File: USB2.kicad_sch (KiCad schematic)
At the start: 5 parts, among them J301 USB_C_Receptacle_USB2.0, U301 RCLAMP0524P

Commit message: Fix schematic ERC errors
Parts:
- U301: footprint Package_SON:USON-10_2.5x1.0mm_P0.5mm -> Package_DFN_QFN:Diodes_UDFN-10_1.0x2.5mm_P0.5mm; symbol Yellow:TPD4EUSB30 -> Hatlabs:RCLAMP0524P
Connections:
- net USB.D+: no longer U301.9 (D1-)
- net USB.D-: no longer U301.10 (D1+)
- net VBUS: no longer U301.7 (D2+)
- net at U301.5: no longer U301.6 (D2-)
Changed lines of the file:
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@@
-			)
-		)
-		(property "Sim.Enable" ""
-			(at 138.43 68.58 0)
-			(effects
-				(font
-					(size 1.27 1.27)
-				)
 			)
 		)
@@
 	)
 	(symbol
-		(lib_name "Yellow:TPD4EUSB30_1")
-		(lib_id "Yellow:TPD4EUSB30")
+		(lib_id "Hatlabs:RCLAMP0524P")
 		(at 163.83 121.92 0)
 		(unit 1)
@@
 			)
 		)
-		(property "Footprint" "Package_SON:USON-10_2.5x1.0mm_P0.5mm"
+		(property "Footprint" "Package_DFN_QFN:Diodes_UDFN-10_1.0x2.5mm_P0.5mm"
 			(at 139.7 132.08 0)
 			(effects
@@
 			)
 		)
-		(property "Description" ""
+		(property "Description" "4-Channel Low Capacitance TVS Diode Array, DFN-10"
 			(at 163.83 121.92 0)
 			(effects
@@
 					(size 1.27 1.27)
 				)
-			)
-		)
-		(property "Sim.Enable" ""
-			(at 163.83 121.92 0)
-			(effects
-				(font
-					(size 1.27 1.27)
-				)
+				(hide yes)
 			)
 		)
@@
 			)
 		)
-		(property "Sim.Enable" ""
-			(at 119.38 66.04 0)
-			(effects
-				(font
-					(size 1.27 1.27)
-				)
-			)
-		)
 		(pin "1"
 		)
@@
 			)
 		)
-		(property "Sim.Enable" ""
-			(at 138.43 66.04 0)
-			(effects
-				(font
-					(size 1.27 1.27)
-				)
-			)
-		)
 		(pin "1"
 		)
@@
 			(at 165.1 76.2 0)
 			(effects
-				(font
-					(size 1.27 1.27)
-				)
-			)
-		)
-		(property "Sim.Enable" ""
-			(at 165.1 76.2 0)
-			(effects

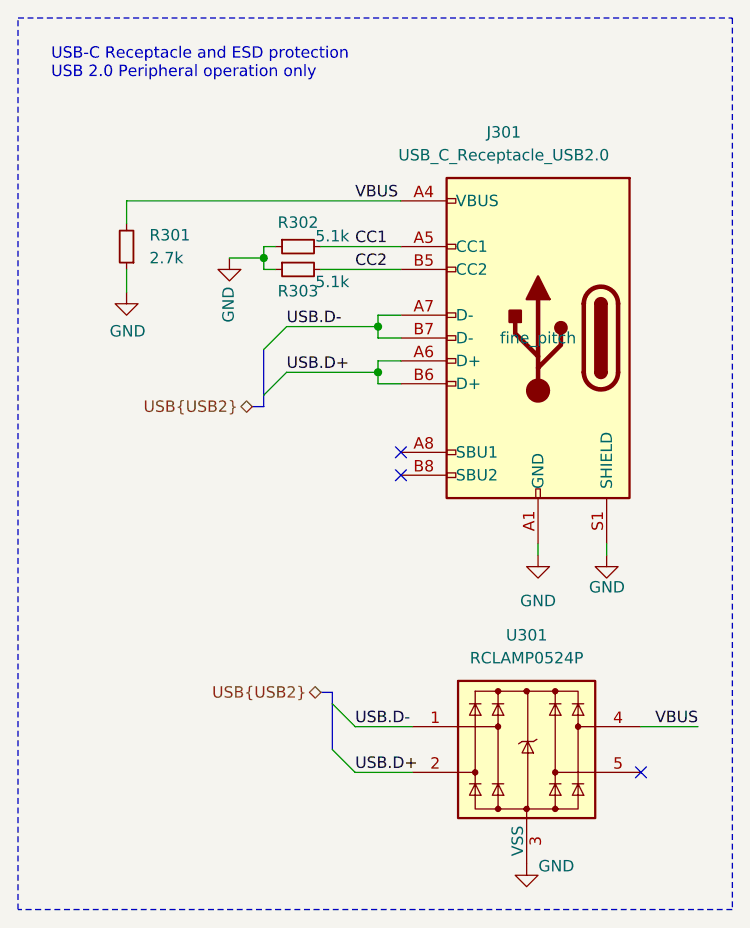
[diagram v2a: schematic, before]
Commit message: Reannotate components
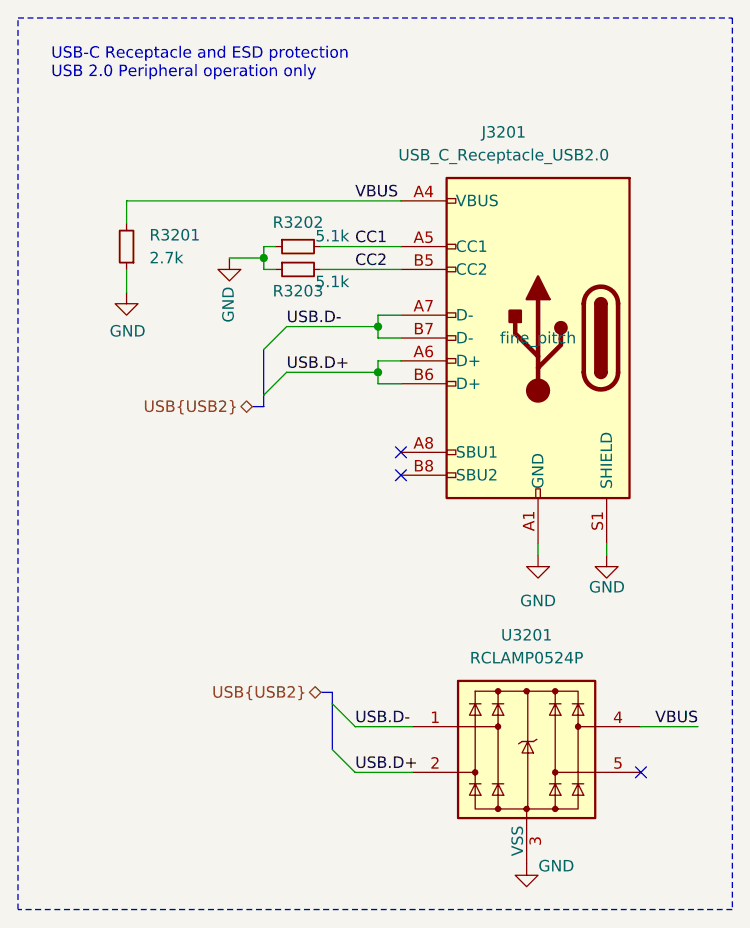
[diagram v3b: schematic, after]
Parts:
- renumbered J301 to J3201, R301 to R3201, R302 to R3202, R303 to R3203, U301 to U3201
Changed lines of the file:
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@@
 		(on_board yes)
 		(dnp no)
-		(property "Reference" "#PWR0301"
+		(property "Reference" "#PWR03202"
 			(at 130.81 73.66 0)
 			(effects
@@
 			(project "HALPI2"
 				(path "/abc482bd-3f17-4d35-80db-1da3dcdb5c27/aa1d8d83-5167-420c-9ee7-3e4dcc942bfc"
-					(reference "#PWR0301")
+					(reference "#PWR03202")
 					(unit 1)
 				)
@@
 		(on_board yes)
 		(dnp no)
-		(property "Reference" "R303"
+		(property "Reference" "R3203"
 			(at 138.43 70.9868 90)
 			(effects
@@
 			(project "HALPI2"
 				(path "/abc482bd-3f17-4d35-80db-1da3dcdb5c27/aa1d8d83-5167-420c-9ee7-3e4dcc942bfc"
-					(reference "R303")
+					(reference "R3203")
 					(unit 1)
 				)
@@
 		(dnp no)
 		(fields_autoplaced yes)
-		(property "Reference" "#PWR0303"
+		(property "Reference" "#PWR03204"
 			(at 165.1 106.68 0)
 			(effects
@@
 			(project "HALPI2"
 				(path "/abc482bd-3f17-4d35-80db-1da3dcdb5c27/aa1d8d83-5167-420c-9ee7-3e4dcc942bfc"
-					(reference "#PWR0303")
+					(reference "#PWR03204")
 					(unit 1)
 				)
@@
 		(on_board yes)
 		(dnp no)
-		(property "Reference" "#PWR0304"
+		(property "Reference" "#PWR03205"
 			(at 172.72 106.68 0)
 			(effects
@@
 			(project "HALPI2"
 				(path "/abc482bd-3f17-4d35-80db-1da3dcdb5c27/aa1d8d83-5167-420c-9ee7-3e4dcc942bfc"
-					(reference "#PWR0304")
+					(reference "#PWR03205")
 					(unit 1)
 				)
@@
 		(on_board yes)
 		(dnp no)
-		(property "Reference" "U301"
+		(property "Reference" "U3201"
 			(at 163.83 109.22 0)
 			(effects
@@
 			(project "HALPI2"
 				(path "/abc482bd-3f17-4d35-80db-1da3dcdb5c27/aa1d8d83-5167-420c-9ee7-3e4dcc942bfc"
-					(reference "U301")
+					(reference "U3201")
 					(unit 1)
 				)
@@
 		(dnp no)
 		(fields_autoplaced yes)
-		(property "Reference" "R301"
+		(property "Reference" "R3201"
 			(at 121.92 64.7699 0)
 			(effects
@@
 			(project "HALPI2"
 				(path "/abc482bd-3f17-4d35-80db-1da3dcdb5c27/aa1d8d83-5167-420c-9ee7-3e4dcc942bfc"
-					(reference "R301")
+					(reference "R3201")
 					(unit 1)
 				)
@@
 		(on_board yes)
 		(dnp no)
-		(property "Reference" "#PWR0302"
+		(property "Reference" "#PWR03201"
 			(at 119.38 77.47 0)
 			(effects
@@
 			(project "HALPI2"
 				(path "/abc482bd-3f17-4d35-80db-1da3dcdb5c27/aa1d8d83-5167-420c-9ee7-3e4dcc942bfc"
-					(reference "#PWR0302")
+					(reference "#PWR03201")
 					(unit 1)
 				)
@@
 		(on_board yes)
 		(dnp no)
-		(property "Reference" "R302"
+		(property "Reference" "R3202"
 			(at 138.43 63.3668 90)
 			(effects
@@
 			(project "HALPI2"
 				(path "/abc482bd-3f17-4d35-80db-1da3dcdb5c27/aa1d8d83-5167-420c-9ee7-3e4dcc942bfc"
-					(reference "R302")
+					(reference "R3202")
 					(unit 1)
 				)
@@
 		(on_board yes)
 		(dnp no)
-		(property "Reference" "J301"
+		(property "Reference" "J3201"
 			(at 161.29 53.34 0)
 			(effects
@@
 			(project "HALPI2"
 				(path "/abc482bd-3f17-4d35-80db-1da3dcdb5c27/aa1d8d83-5167-420c-9ee7-3e4dcc942bfc"
-					(reference "J301")
+					(reference "J3201")
 					(unit 1)
 				)
@@
 		(on_board yes)
 		(dnp no)
-		(property "Reference" "#PWR0305"
+		(property "Reference" "#PWR03203"
 			(at 163.83 140.97 0)
 			(effects
@@
 			(project "HALPI2"
 				(path "/abc482bd-3f17-4d35-80db-1da3dcdb5c27/aa1d8d83-5167-420c-9ee7-3e4dcc942bfc"
-					(reference "#PWR0305")
-					(unit 1)
-				)
+					(reference "#PWR03203")
+					(unit 1)
+				)

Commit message: Most DRC errors fixed
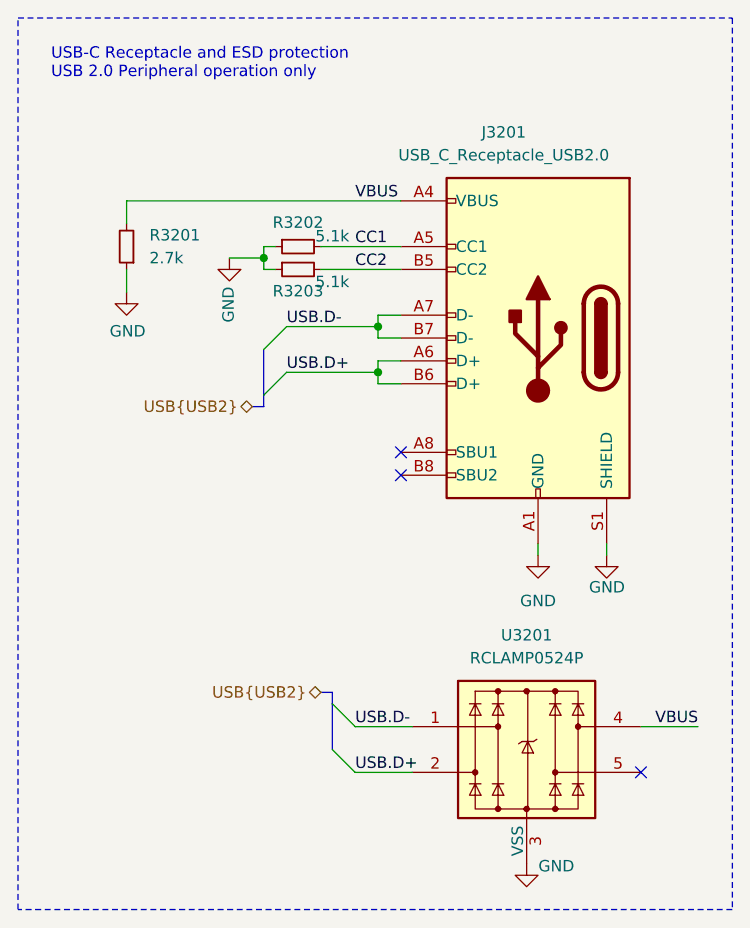
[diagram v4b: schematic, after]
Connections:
- net USB.D+: now also U3201.9 (NC)
- net USB.D-: now also U3201.10 (NC)
- net VBUS: now also U3201.7 (NC)
- net at U3201.5: now also U3201.6 (NC)
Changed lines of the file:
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@@
 					(size 1.27 1.27)
 				)
+				(hide yes)
 			)
 		)
